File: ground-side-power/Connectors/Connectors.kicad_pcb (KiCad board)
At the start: 2 copper layers, 11 parts, among them J15 To Router, J16 To RLCS, J17 To DAQ Laptop, J18 Conn_01x02_Female, J19 Conn_01x02_Female, J20 To Ethernet, J21 To 5V M12, J22 To DAQ, J23 Extra M12, J24 Extra M12, J25 Extra M12

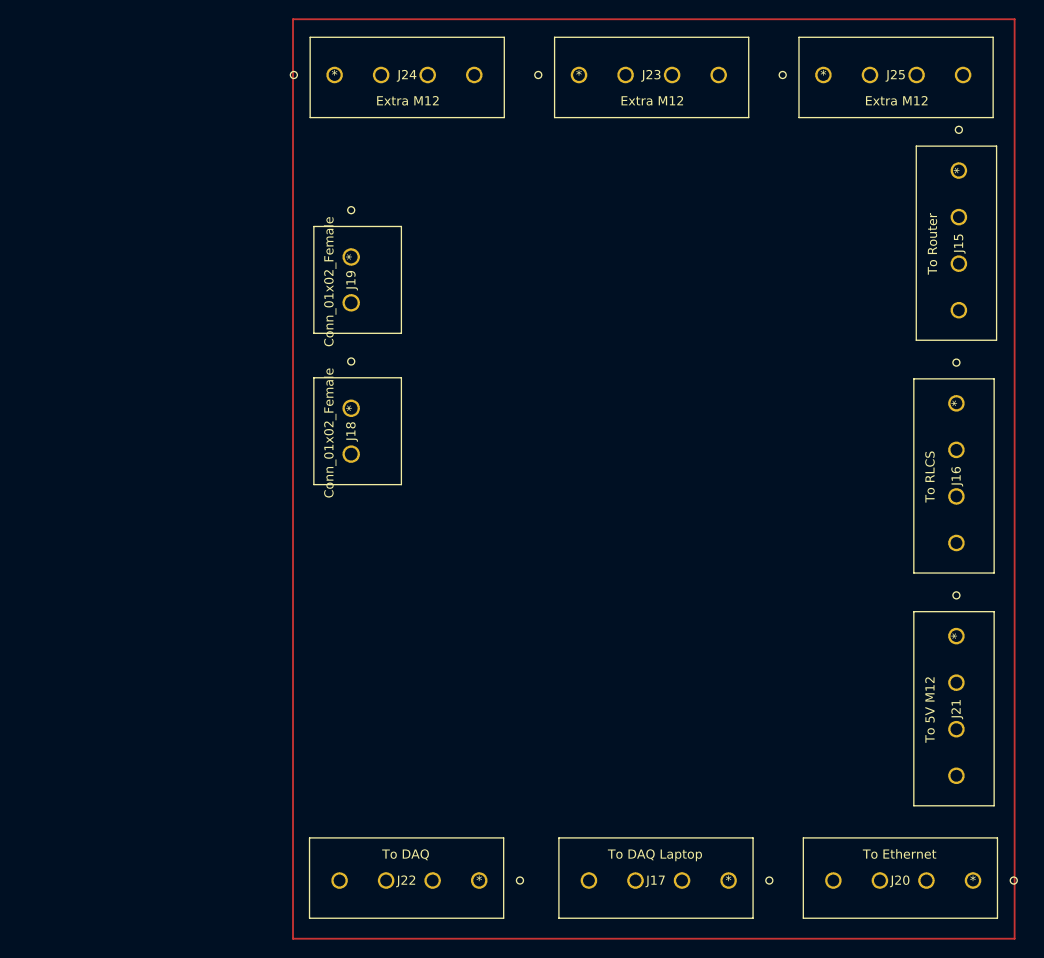
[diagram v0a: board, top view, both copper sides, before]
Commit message: Added Fan Headers + Thermistor
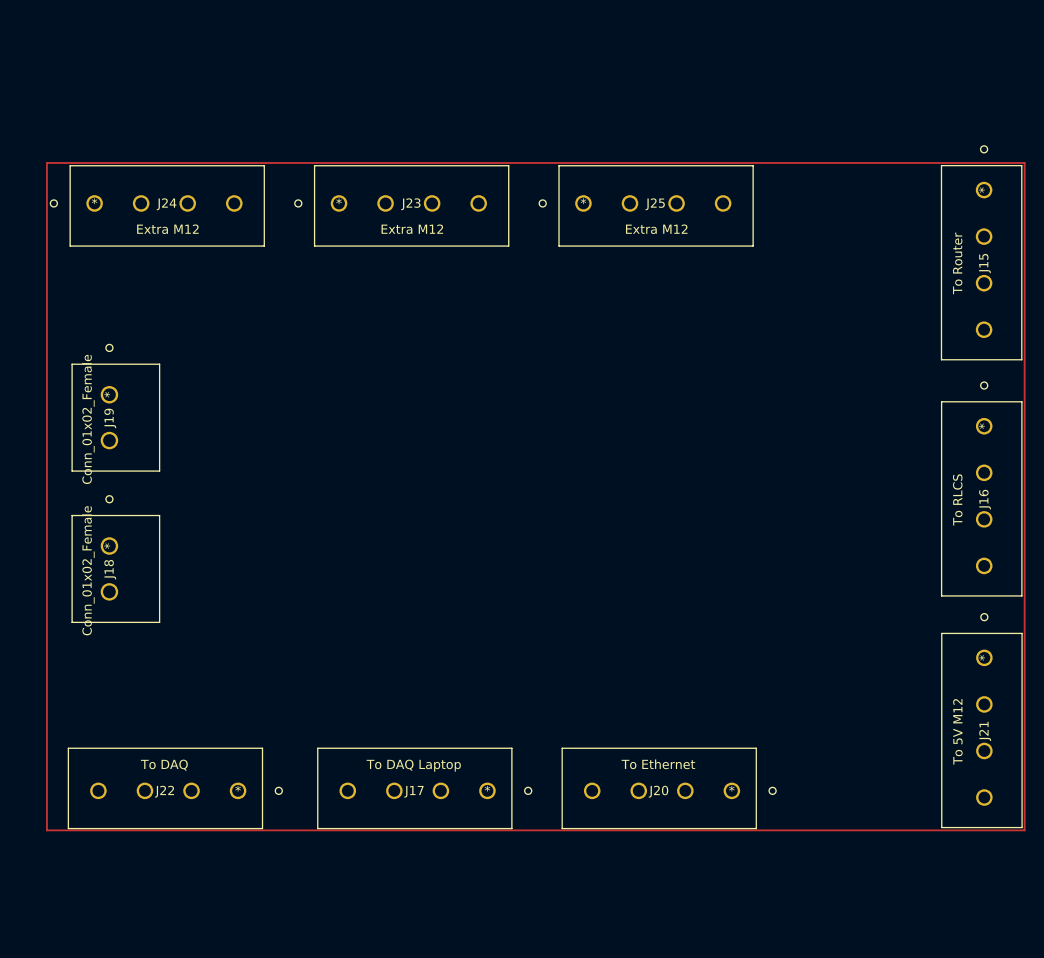
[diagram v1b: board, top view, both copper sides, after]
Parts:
- moved J18 30.4 mm to (98.1, 105.7)
- moved J19 30.4 mm to (98.1, 89.2)
- moved J23 29.7 mm to (123.1, 68.4)
- moved J24 29.7 mm to (96.5, 68.4)
- moved J25 29.7 mm to (149.8, 68.4)
- moved J17 28.1 mm to (139.3, 132.5)
- moved J22 28.1 mm to (112.1, 132.5)
- moved J20 28.1 mm to (166.0, 132.5)
- moved J16 3.93 mm to (193.5, 92.7)
- moved J21 3.86 mm to (193.5, 117.9)
- moved J15 3.48 mm to (193.5, 66.9)

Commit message: PCB Layout First Draft
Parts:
- added M2: Fan_PC_Chassis, Connector:FanPinHeader_1x03_P2.54mm_Vertical, F.Cu at (178.6, 70.5)
- moved J25 17.6 mm to (167.1, 71.6), turned to 180 degrees
- moved J23 16.9 mm to (139.8, 71.6), turned to 180 degrees
- moved J24 16.4 mm to (112.6, 71.6), turned to 180 degrees
- moved J21 16.4 mm to (189.5, 133.8), turned to 90 degrees
- moved J15 16.4 mm to (189.5, 82.7), turned to 90 degrees
- moved J16 16.1 mm to (189.5, 108.2), turned to 90 degrees
- moved J22 15.1 mm to (97.5, 128.8), turned to 0 degrees
- moved J17 14.9 mm to (124.9, 128.8), turned to 0 degrees
- moved J20 14.6 mm to (151.8, 128.8), turned to 0 degrees
- moved J18 1.04 mm to (99.1, 105.7)
- moved J19 1.04 mm to (99.1, 89.2)
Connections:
- J15 pad 1: (no net) -> +24V
- J15 pad 2: (no net) -> +12V
- J15 pad 3: (no net) -> +5V
- J15 pad 4: (no net) -> GND
- J16 pad 1: (no net) -> +24V
- J16 pad 2: (no net) -> +12V
- J16 pad 3: (no net) -> +5V
- J16 pad 4: (no net) -> GND
- J17 pad 1: (no net) -> +24V
- J17 pad 2: (no net) -> +12V
- J17 pad 3: (no net) -> +5V
- J17 pad 4: (no net) -> GND
- J18 pad 1: (no net) -> GND
- J18 pad 2: (no net) -> +24V
- J19 pad 1: (no net) -> +5V
- J19 pad 2: (no net) -> +12V
- J20 pad 1: (no net) -> +24V
- J20 pad 2: (no net) -> +12V
- J20 pad 3: (no net) -> +5V
- J20 pad 4: (no net) -> GND
- J21 pad 1: (no net) -> +24V
- J21 pad 2: (no net) -> +12V
- J21 pad 3: (no net) -> +5V
- J21 pad 4: (no net) -> GND
- J22 pad 1: (no net) -> +24V
- J22 pad 2: (no net) -> +12V
- J22 pad 3: (no net) -> +5V
- J22 pad 4: (no net) -> GND
- J23 pad 1: (no net) -> +24V
- J23 pad 2: (no net) -> +12V
- J23 pad 3: (no net) -> +5V
- J23 pad 4: (no net) -> GND
- J24 pad 1: (no net) -> +24V
- J24 pad 2: (no net) -> +12V
- J24 pad 3: (no net) -> +5V
- J24 pad 4: (no net) -> GND
- J25 pad 1: (no net) -> +24V
- J25 pad 2: (no net) -> +12V
- J25 pad 3: (no net) -> +5V
- J25 pad 4: (no net) -> GND
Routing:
- net +5V: track 0.00 -> 380.6 mm
- net +24V: track 0.00 -> 364.0 mm
- added copper zone on B.Cu, net +12V
- added copper zone on F.Cu, net GND
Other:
- board outline added: 106.7 x 72.8 mm
- board text added: "+12"
- board text added: "+24"
- board text added: "+5"
- board text added: "0"

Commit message: Resolved Final Issues
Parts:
- added ?: , , F.Cu at (95.2, 129.9)
- added ?: , , F.Cu at (183.6, 70.4)
- added ?: , , F.Cu at (183.6, 129.9)
- added G***: LOGO, rlcs:rocketry_logo_small, F.Cu at (106.3, 72.4)
- added REF**: MountingHole_3.2mm_M3_Pad, MountingHole:MountingHole_3.2mm_M3_Pad, F.Cu at (95.2, 70.4)
- J15, J16, J17, J20, J21, J22, J23, J24, J25: footprint GSP:EB21A-04-D -> GSP:CUI_TB008A-508-04BE
- J18: footprint GSP:OSTTA020161 -> GSP:1935310
- J19: footprint GSP:OSTTA020161 -> GSP:1935323
- moved M2 94.7 mm to (104.3, 129.2), turned to 0 degrees
- moved J25 64.4 mm to (119.5, 114.9), turned to -90 degrees
- moved J21 62.2 mm to (142.9, 92.6), turned to -90 degrees
- moved J20 59.1 mm to (142.8, 70.4), turned to -90 degrees
- moved J22 47.4 mm to (142.8, 114.9), turned to -90 degrees
- moved J17 43.5 mm to (166.2, 114.9), turned to -90 degrees
- moved J16 28.0 mm to (166.2, 92.6), turned to -90 degrees
- moved J15 26.4 mm to (166.2, 70.4), turned to -90 degrees
- moved J24 22.1 mm to (119.6, 92.6), turned to -90 degrees
- moved J23 20.3 mm to (119.5, 70.4), turned to -90 degrees
- moved J19 17.5 mm to (102.2, 106.4), turned to 90 degrees
- moved J18 17.4 mm to (102.2, 88.5), turned to 90 degrees
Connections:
- J18 pad 1: GND -> +12V
- J18 pad 2: +24V -> GND
- J19 pad 1: +5V -> +24V
- J19 pad 2: +12V -> GND
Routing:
- net +5V: track 380.6 -> 0.00 mm
- net +24V: track 364.0 -> 0.00 mm
- net GND: track 0.00 -> 244.5 mm
- net +12V: track 0.00 -> 233.1 mm
- added copper zone on F.Cu, net +24V
- added copper zone on B.Cu, net +5V
- removed copper zone on B.Cu, net +12V
- removed copper zone on F.Cu, net GND
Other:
- board size 106.7 x 72.8 mm -> 97.7 x 68.7 mm
- board text added: "Ground Side Power Connector Board Domenic Hampson Elias Kountouris"

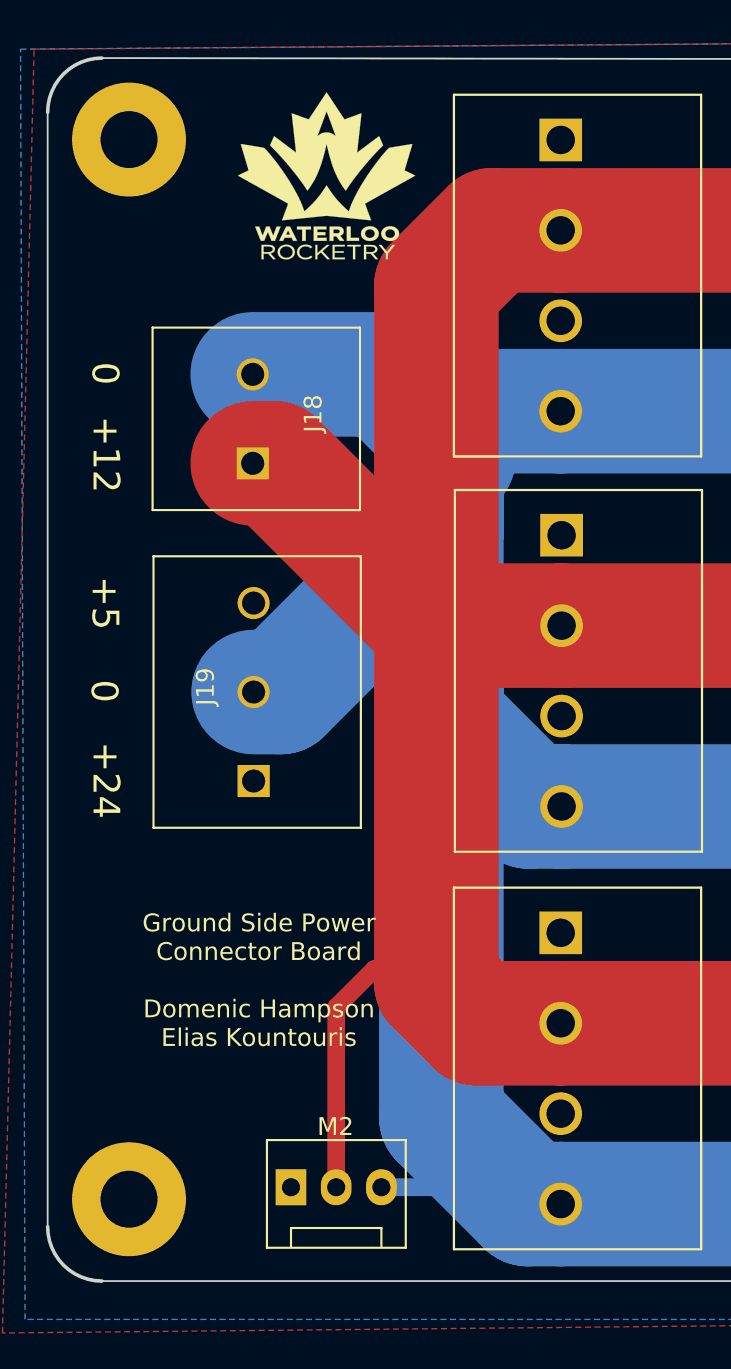
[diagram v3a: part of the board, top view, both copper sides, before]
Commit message: Silkscreen and current sense changes
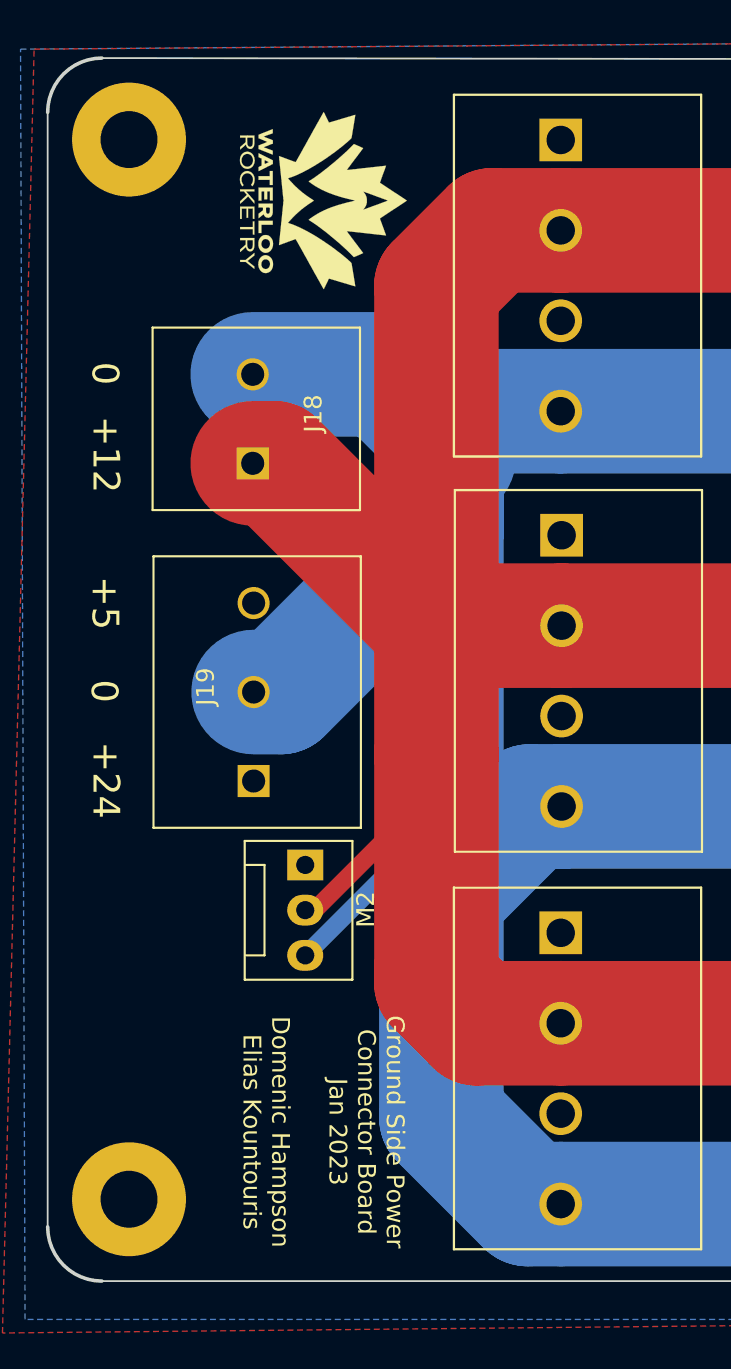
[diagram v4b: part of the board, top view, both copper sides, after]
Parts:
- moved M2 18.1 mm to (105.2, 111.1), turned to -90 degrees
- moved G*** 1.40 mm to (106.2, 73.8), turned to -90 degrees
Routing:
- net +12V: track 233.1 -> 228.5 mm
- net GND: track 244.5 -> 246.2 mm
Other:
- board text added: "Ground Side Power Connector Board Jan 2023 Domenic Hampson Elias Kountouris"
- board text removed: "Ground Side Power Connector Board Domenic Hampson Elias Kountouris"
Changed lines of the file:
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@@
   )
   (footprint "rlcs:rocketry_logo_small" (layer "F.Cu")
-    (at 106.35 72.4)
+    (at 106.172221 73.787 -90)
     (attr through_hole)
-    (fp_text reference "G***" (at -0.127 -2.0574) (layer "F.SilkS") hide
+    (fp_text reference "G***" (at -0.127 -2.0574 90) (layer "F.SilkS") hide
       (effects (font (size 1.524 1.524) (thickness 0.3)))
     )
-    (fp_text value "LOGO" (at 0.75 0) (layer "F.SilkS") hide
+    (fp_text value "LOGO" (at 0.75 0 90) (layer "F.SilkS") hide
       (effects (font (size 1.524 1.524) (thickness 0.3)))
     )
@@
   )
   (footprint "Connector:FanPinHeader_1x03_P2.54mm_Vertical" (layer "F.Cu")
-    (at 104.35 129.225)
+    (at 105.15 111.115 -90)
     (descr "3-pin CPU fan Through hole pin header, see http://www.formfactors.org/developer%5Cspecs%5Crev1_2_public.pdf")
     (tags "pin header 3-pin CPU fan")
@@
     (property "Sheetname" "")
     (attr through_hole)
-    (fp_text reference "M2" (at 2.5 -3.4) (layer "F.SilkS")
+    (fp_text reference "M2" (at 2.5 -3.4 90) (layer "F.SilkS")
       (effects (font (size 1 1) (thickness 0.15)))
     )
-    (fp_text value "Fan_PC_Chassis" (at 2.55 4.5) (layer "F.Fab") hide
+    (fp_text value "Fan_PC_Chassis" (at 2.55 4.5 90) (layer "F.Fab") hide
       (effects (font (size 1 1) (thickness 0.15)))
     )
-    (fp_text user "${REFERENCE}" (at 2.45 1.8) (layer "F.Fab") hide
+    (fp_text user "${REFERENCE}" (at 2.45 1.8 90) (layer "F.Fab") hide
       (effects (font (size 1 1) (thickness 0.15)))
     )
@@
     (fp_line (start 6.35 -2.55) (end 6.35 3.3) (layer "F.Fab") (width 0.1))
     (fp_line (start -1.25 3.3) (end -1.25 -2.55) (layer "F.Fab") (width 0.1))
-    (pad "1" thru_hole rect (at 0 0 90) (size 2.03 1.73) (drill 1.02) (layers *.Cu *.Mask)
+    (pad "1" thru_hole rect (at 0 0) (size 2.03 1.73) (drill 1.02) (layers *.Cu *.Mask)
       (net 5 "unconnected-(M2-Pad1)") (pinfunction "Tacho") (pintype "passive+no_connect"))
-    (pad "2" thru_hole oval (at 2.54 0 90) (size 2.03 1.73) (drill 1.02) (layers *.Cu *.Mask)
+    (pad "2" thru_hole oval (at 2.54 0) (size 2.03 1.73) (drill 1.02) (layers *.Cu *.Mask)
       (net 2 "+12V") (pinfunction "+") (pintype "passive"))
-    (pad "3" thru_hole oval (at 5.08 0 90) (size 2.03 1.73) (drill 1.02) (layers *.Cu *.Mask)
+    (pad "3" thru_hole oval (at 5.08 0) (size 2.03 1.73) (drill 1.02) (layers *.Cu *.Mask)
       (net 4 "GND") (pinfunction "-") (pintype "passive"))
     (model "${KICAD6_3DMODEL_DIR}/Connector.3dshapes/FanPinHeader_1x03_P2.54mm_Vertical.wrl"
@@
     (effects (font (size 1.5 1.5) (thickness 0.3)))
   )
-  (gr_text "Ground Side Power\nConnector Board\n\nDomenic Hampson \nElias Kountouris" (at 102.55 117.602) (layer "F.SilkS")
+  (gr_text "Ground Side Power\nConnector Board\nJan 2023\n\nDomenic Hampson \nElias Kountouris" (at 106.172 126.111 270) (layer "F.SilkS")
     (effects (font (size 1 1) (thickness 0.15)))
   )
@@
     (effects (font (size 1.5 1.5) (thickness 0.3)))
   )
-  (segment (start 112.52 97.67) (end 112.52 116.97) (width 7) (layer "F.Cu") (net 2))
+  (segment (start 112.52 97.67) (end 112.52 104.904) (width 7) (layer "F.Cu") (net 2))
   (segment (start 103.4 88.55) (end 112.52 97.67) (width 7) (layer "F.Cu") (net 2))
+  (segment (start 105.15 113.655) (end 105.674 113.655) (width 0.25) (layer "F.Cu") (net 2))
   (segment (start 112.52 97.67) (end 119.555 97.67) (width 7) (layer "F.Cu") (net 2))
   (segment (start 112.52 117.745) (end 114.785 120.01) (width 7) (layer "F.Cu") (net 2))
@@
   (segment (start 119.555 97.67) (end 142.8775 97.67) (width 7) (layer "F.Cu") (net 2))
   (segment (start 112.52 116.97) (end 112.52 117.745) (width 7) (layer "F.Cu") (net 2))
+  (segment (start 105.674 113.655) (end 112.52 106.809) (width 1) (layer "F.Cu") (net 2))
   (segment (start 166.15 75.46) (end 142.8275 75.46) (width 7) (layer "F.Cu") (net 2))
   (segment (start 102.199999 88.55) (end 103.4 88.55) (width 7) (layer "F.Cu") (net 2))
@@
   (segment (start 142.8275 120.01) (end 166.15 120.01) (width 7) (layer "F.Cu") (net 2))
   (segment (start 142.8775 97.67) (end 166.2 97.67) (width 7) (layer "F.Cu") (net 2))
-  (segment (start 109.03 116.97) (end 112.52 116.97) (width 1) (layer "F.Cu") (net 2))
-  (segment (start 106.89 129.225) (end 106.89 119.11) (width 1) (layer "F.Cu") (net 2))
   (segment (start 119.505 120.01) (end 142.8275 120.01) (width 7) (layer "F.Cu") (net 2))
   (segment (start 119.505 75.46) (end 142.8275 75.46) (width 7) (layer "F.Cu") (net 2))
+  (segment (start 112.52 104.904) (end 112.52 116.97) (width 7) (layer "F.Cu") (net 2))
+  (segment (start 112.52 106.809) (end 112.52 104.904) (width 0.25) (layer "F.Cu") (net 2))
   (segment (start 112.52 97.67) (end 112.52 78.58) (width 7) (layer "F.Cu") (net 2))
-  (segment (start 106.89 119.11) (end 109.03 116.97) (width 1) (layer "F.Cu") (net 2))
   (segment (start 112.8 125.314647) (end 117.655353 130.17) (width 7) (layer "B.Cu") (net 4))
-  (segment (start 112.8 100.15) (end 112.8 102.924647) (width 7) (layer "B.Cu") (net 4))
   (segment (start 142.8275 85.62) (end 166.15 85.62) (width 7) (layer "B.Cu") (net 4))
+  (segment (start 105.15 116.195) (end 112.8 108.545) (width 1) (layer "B.Cu") (net 4))
   (segment (start 119.555 107.83) (end 142.8775 107.83) (width 7) (layer "B.Cu") (net 4))
   (segment (start 112.8 86.8) (end 113.98 85.62) (width 7) (layer "B.Cu") (net 4))
   (segment (start 142.8275 130.17) (end 166.15 130.17) (width 7) (layer "B.Cu") (net 4))
   (segment (start 109.55 83.55) (end 113.5 87.5) (width 7) (layer "B.Cu") (net 4))
-  (segment (start 117.705353 107.83) (end 119.555 107.83) (width 7) (layer "B.Cu") (net 4))
   (segment (start 113.98 85.62) (end 119.505 85.62) (width 7) (layer "B.Cu") (net 4))
   (segment (start 102.249999 101.4) (end 103.757786 101.4) (width 7) (layer "B.Cu") (net 4))
   (segment (start 112.8 100.15) (end 112.8 90.3) (width 7) (layer "B.Cu") (net 4))
   (segment (start 117.655353 130.17) (end 119.505 130.17) (width 7) (layer "B.Cu") (net 4))
-  (segment (start 112.8 102.924647) (end 117.705353 107.83) (width 7) (layer "B.Cu") (net 4))
   (segment (start 113.5 87.5) (end 113.5 88.2) (width 7) (layer "B.Cu") (net 4))
   (segment (start 142.8775 107.83) (end 166.2 107.83) (width 7) (layer "B.Cu") (net 4))
-  (segment (start 109.43 129.225) (end 116.710353 129.225) (width 1) (layer "B.Cu") (net 4))
+  (segment (start 112.8 100.15) (end 112.8 107.672) (width 7) (layer "B.Cu") (net 4))
+  (segment (start 112.8 107.672) (end 112.8 125.314647) (width 7) (layer "B.Cu") (net 4))
   (segment (start 112.8 92.357786) (end 112.8 90.3) (width 7) (layer "B.Cu") (net 4))
+  (segment (start 112.8 108.545) (end 112.8 107.672) (width 0.25) (layer "B.Cu") (net 4))
+  (segment (start 117.77 107.83) (end 112.8 112.8) (width 7) (layer "B.Cu") (net 4))
   (segment (start 103.757786 101.4) (end 112.8 92.357786) (width 7) (layer "B.Cu") (net 4))
-  (segment (start 112.8 100.15) (end 112.8 125.314647) (width 7) (layer "B.Cu") (net 4))
   (segment (start 119.505 130.17) (end 142.8275 130.17) (width 7) (layer "B.Cu") (net 4))
+  (segment (start 119.555 107.83) (end 117.77 107.83) (width 7) (layer "B.Cu") (net 4))
   (segment (start 116.710353 129.225) (end 117.655353 130.17) (width 1) (layer "B.Cu") (net 4))
   (segment (start 119.505 85.62) (end 142.8275 85.62) (width 7) (layer "B.Cu") (net 4))
@@
   (segment (start 112.8 90.3) (end 112.8 86.8) (width 7) (layer "B.Cu") (net 4))
   (zone (net 1) (net_name "+24V") (layer "F.Cu") (hatch edge 0.508)
-    (connect_pads (clearance 0.508))
+    (connect_pads yes (clearance 0.508))
     (min_thickness 0.254) (filled_areas_thickness no)
     (fill yes (thermal_gap 0.508) (thermal_bridge_width 0.508))
@@
   )
   (zone (net 3) (net_name "+5V") (layer "B.Cu") (hatch edge 0.508)
-    (connect_pads (clearance 0.508))
+    (connect_pads yes (clearance 0.508))
     (min_thickness 0.254) (filled_areas_thickness no)
     (fill yes (thermal_gap 0.508) (thermal_bridge_width 0.508))
